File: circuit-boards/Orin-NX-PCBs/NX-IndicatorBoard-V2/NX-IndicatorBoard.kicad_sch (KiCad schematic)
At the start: 12 parts, among them J1 NX Expansion, J2 CAN1, J3 CAN1, J4 CAN2, J5 CAN2, J6 PC LED, P1 Samtec 40 pin Elevated Socket

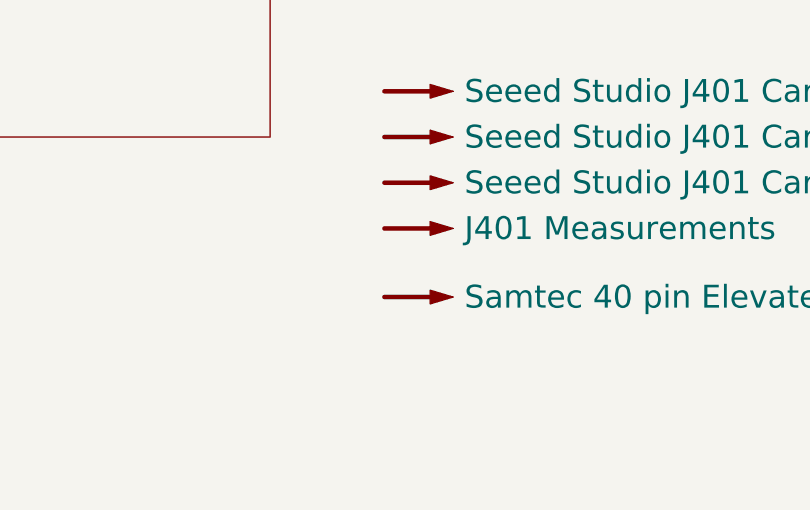
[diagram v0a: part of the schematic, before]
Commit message: Check in of NX Adapter and Indicator boards.  Complete pending review
Signed-off-by: Scott <sgberman1@gmail.com>
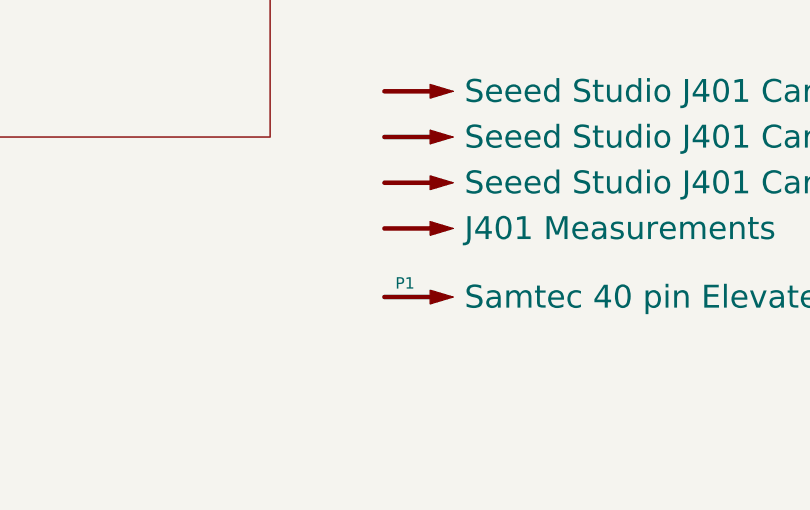
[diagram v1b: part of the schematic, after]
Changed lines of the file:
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@@
 	(title_block
 		(title "NX Indicator Board V2")
-		(date "2024-07-14")
+		(date "2024-07-21")
 		(rev "2")
 		(company "971 Spartan Robotics")
@@
 		(dnp no)
 		(property "Reference" "P1"
-			(at 237.49 199.644 0)
-			(effects
-				(font
-					(size 1.27 1.27)
-				)
-				(hide yes)
-			)
-		)
+			(at 235.966 200.406 0)
+			(effects
+				(font
+					(size 1.27 1.27)
+				)
+			)
+		)

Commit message: Intermediate checkin of NX-Indicator-board
Signed-off-by: Scott Berman <scott.berman@bluerivertech.com>
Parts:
- removed H1, H4: MountingHole, MountingHole:MountingHole_2.7mm_M2.5_Pad, symbol Mechanical:MountingHole
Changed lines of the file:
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@@
-	)
-	(symbol
-		(lib_id "Mechanical:MountingHole")
-		(at 148.59 200.66 0)
-		(unit 1)
-		(exclude_from_sim no)
-		(in_bom no)
-		(on_board yes)
-		(dnp no)
-		(fields_autoplaced yes)
-		(property "Reference" "H4"
-			(at 151.13 199.39 0)
-			(effects
-				(font
-					(size 1.27 1.27)
-				)
-				(justify left)
-			)
-		)
-		(property "Value" "MountingHole"
-			(at 151.13 201.93 0)
-			(effects
-				(font
-					(size 1.27 1.27)
-				)
-				(justify left)
-			)
-		)
-		(property "Footprint" "MountingHole:MountingHole_2.7mm_M2.5_Pad"
-			(at 148.59 200.66 0)
-			(effects
-				(font
-					(size 1.27 1.27)
-				)
-				(hide yes)
-			)
-		)
-		(property "Datasheet" "~"
-			(at 148.59 200.66 0)
-			(effects
-				(font
-					(size 1.27 1.27)
-				)
-				(hide yes)
-			)
-		)
-		(property "Description" ""
-			(at 148.59 200.66 0)
-			(effects
-				(font
-					(size 1.27 1.27)
-				)
-				(hide yes)
-			)
-		)
-		(instances
-			(project "NX-IndicatorBoard"
-				(path "/b2b9b2ba-ad3f-4e65-98f2-b291a62e1006"
-					(reference "H4")
-					(unit 1)
-				)
-			)
-		)
 	)
 	(symbol
@@
 					(unit 1)
 				)
-			)
-		)
-	)
-	(symbol
-		(lib_id "Mechanical:MountingHole")
-		(at 148.59 194.31 0)
-		(unit 1)
-		(exclude_from_sim no)
-		(in_bom no)
-		(on_board yes)
-		(dnp no)
-		(fields_autoplaced yes)
-		(property "Reference" "H1"
-			(at 151.13 193.04 0)
-			(effects
-				(font
-					(size 1.27 1.27)
-				)
-				(justify left)
-			)
-		)
-		(property "Value" "MountingHole"
-			(at 151.13 195.58 0)
-			(effects
-				(font
-					(size 1.27 1.27)
-				)
-				(justify left)
-			)
-		)
-		(property "Footprint" "MountingHole:MountingHole_2.7mm_M2.5_Pad"
-			(at 148.59 194.31 0)
-			(effects
-				(font
-					(size 1.27 1.27)
-				)
-				(hide yes)
-			)
-		)
-		(property "Datasheet" "~"
-			(at 148.59 194.31 0)
-			(effects
-				(font
-					(size 1.27 1.27)
-				)
-				(hide yes)
-			)
-		)
-		(property "Description" ""
-			(at 148.59 194.31 0)
-			(effects
-				(font
-					(size 1.27 1.27)
-				)
-				(hide yes)
-			)
-		)
-		(instances
-			(project "NX-IndicatorBoard"
-				(path "/b2b9b2ba-ad3f-4e65-98f2-b291a62e1006"
-					(reference "H1")
-					(unit 1)
-				)

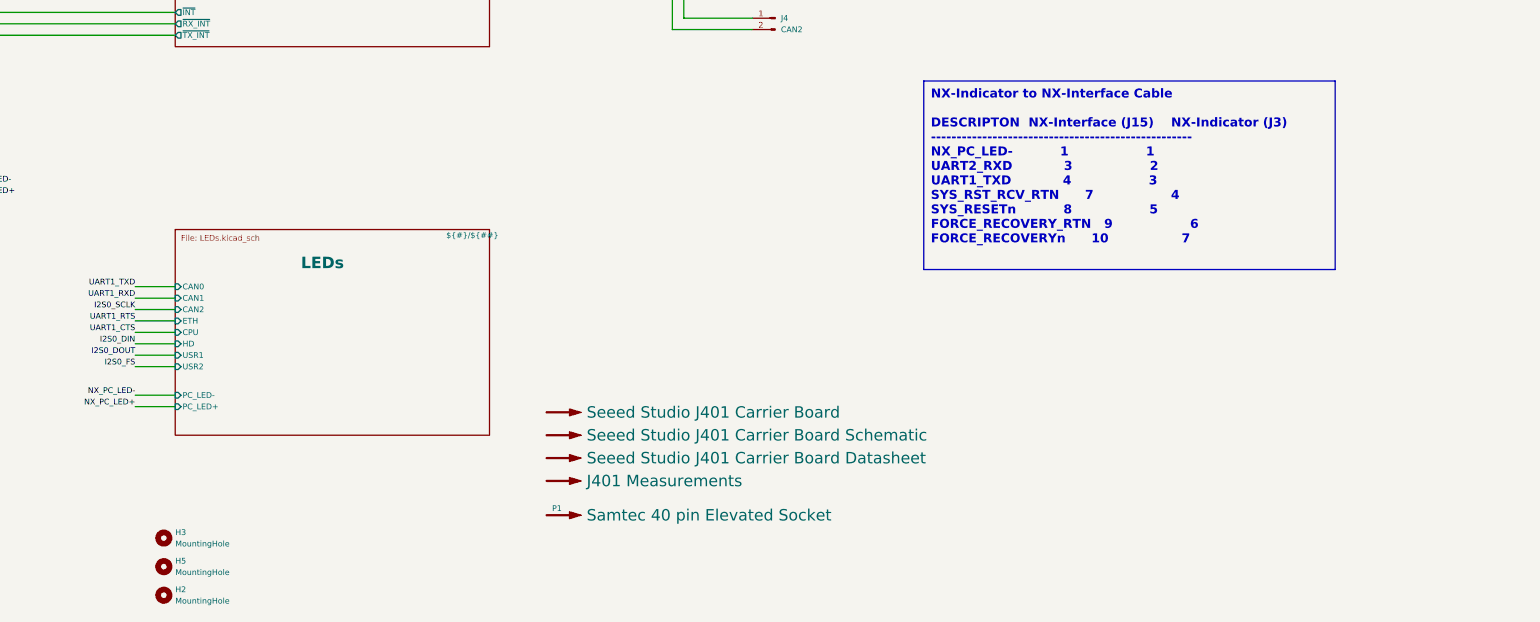
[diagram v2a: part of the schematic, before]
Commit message: Checkin of NX Indicator board 2x CAN FD + 6 LEDs
Signed-off-by: Scott <sgberman1@gmail.com>
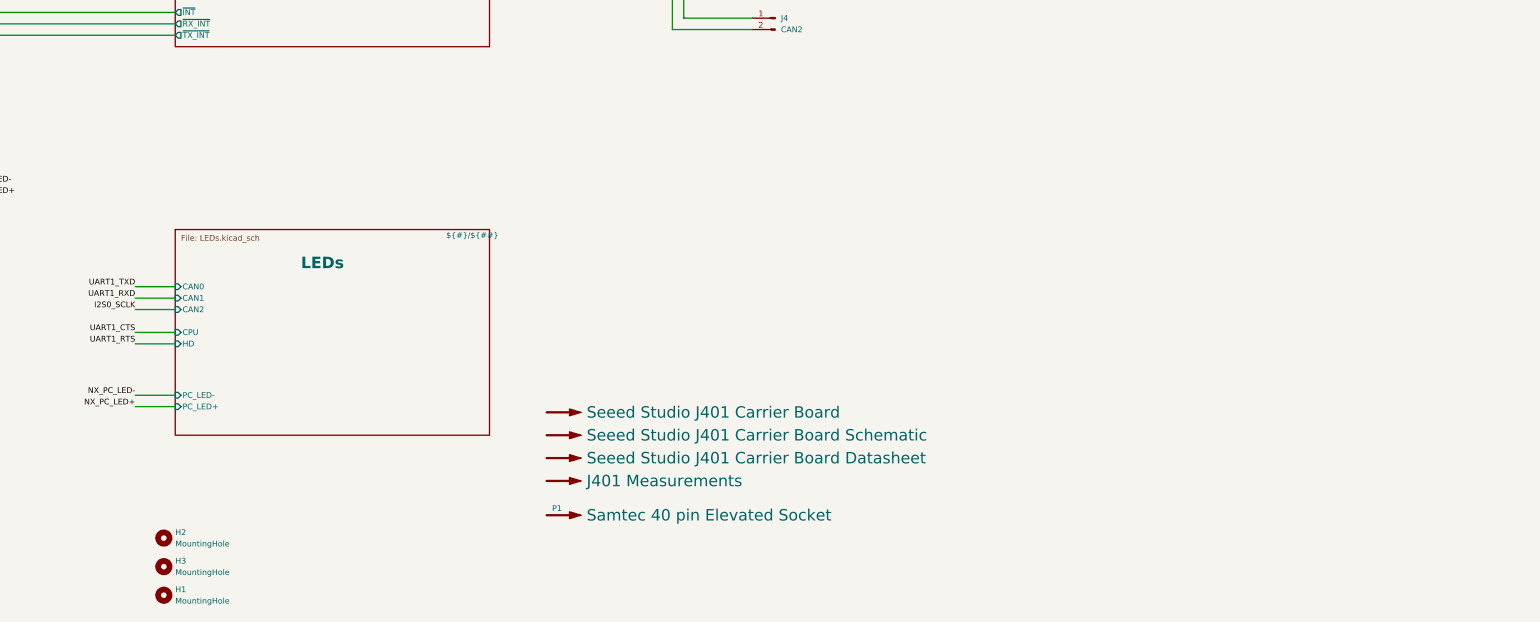
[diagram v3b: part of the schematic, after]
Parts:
- renumbered H2 to H1, H3 to H2, H5 to H3
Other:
- sheet LEDs ports: added none; removed ETH, USR1, USR2
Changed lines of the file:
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@@
 	(title_block
 		(title "NX Indicator Board V2")
-		(date "2024-07-21")
+		(date "2024-07-28")
 		(rev "2")
 		(company "971 Spartan Robotics")
@@
 	(wire
 		(pts
-			(xy 142.24 168.91) (xy 151.13 168.91)
-		)
-		(stroke
-			(width 0)
-			(type default)
-		)
-	)
-	(wire
-		(pts
 			(xy 261.62 86.36) (xy 279.4 86.36)
 		)
@@
 	(wire
 		(pts
-			(xy 142.24 158.75) (xy 151.13 158.75)
-		)
-		(stroke
-			(width 0)
-			(type default)
-		)
-	)
-	(wire
-		(pts
 			(xy 81.28 165.1) (xy 91.44 165.1)
 		)
@@
 	(wire
 		(pts
-			(xy 142.24 166.37) (xy 151.13 166.37)
-		)
-		(stroke
-			(width 0)
-			(type default)
-		)
-	)
-	(wire
-		(pts
 			(xy 104.14 40.64) (xy 151.13 40.64)
 		)
@@
 		)
 	)
-	(text_box "NX-Indicator to NX-Interface Cable\n\nDESCRIPTON  NX-Interface (J15)    NX-Indicator (J3)\n---------------------------------------------------\nNX_PC_LED-           1                  1\nUART2_RXD            3                  2\nUART1_TXD            4                  3\nSYS_RST_RCV_RTN      7                  4\nSYS_RESETn           8                  5\nFORCE_RECOVERY_RTN   9                  6\nFORCE_RECOVERYn      10                 7\n"
-		(exclude_from_sim no)
-		(at 317.5 105.41 0)
-		(size 91.44 41.91)
-		(stroke
-			(width 0)
-			(type default)
-		)
-		(fill
-			(type none)
-		)
-		(effects
-			(font
-				(face "FreeMono")
-				(size 2 2)
-				(bold yes)
-			)
-			(justify left top)
-		)
-	)
 	(label "I2C1_SCL"
 		(at 64.77 170.18 180)
@@
 		)
 	)
+	(label "UART1_RTS"
+		(at 142.24 163.83 180)
+		(fields_autoplaced yes)
+		(effects
+			(font
+				(size 1.27 1.27)
+			)
+			(justify right bottom)
+		)
+	)
 	(label "SPI1_CS0"
 		(at 104.14 86.36 180)
@@
 		)
 	)
-	(label "I2S0_FS"
-		(at 142.24 168.91 180)
-		(fields_autoplaced yes)
-		(effects
-			(font
-				(size 1.27 1.27)
-			)
-			(justify right bottom)
-		)
-	)
 	(label "SPI1_CS1"
 		(at 85.09 182.88 0)
@@
 		)
 	)
-	(label "I2S0_DIN"
-		(at 142.24 163.83 180)
-		(fields_autoplaced yes)
-		(effects
-			(font
-				(size 1.27 1.27)
-			)
-			(justify right bottom)
-		)
-	)
 	(label "CAN2_L"
 		(at 278.13 83.82 180)
@@
 		)
 	)
-	(label "I2S0_DOUT"
-		(at 142.24 166.37 180)
-		(fields_autoplaced yes)
-		(effects
-			(font
-				(size 1.27 1.27)
-			)
-			(justify right bottom)
-		)
-	)
 	(label "NX_PC_LED-"
 		(at 142.24 175.26 180)
@@
 		)
 	)
-	(label "UART1_RTS"
-		(at 142.24 158.75 180)
-		(fields_autoplaced yes)
-		(effects
-			(font
-				(size 1.27 1.27)
-			)
-			(justify right bottom)
-		)
-	)
 	(label "NX_PC_LED+"
 		(at 104.14 130.81 0)
@@
 		(dnp no)
 		(fields_autoplaced yes)
-		(property "Reference" "H5"
+		(property "Reference" "H3"
 			(at 151.13 212.09 0)
 			(effects
@@
 			(project "NX-IndicatorBoard"
 				(path "/b2b9b2ba-ad3f-4e65-98f2-b291a62e1006"
-					(reference "H5")
+					(reference "H3")
 					(unit 1)
 				)
@@
 		(dnp no)
 		(fields_autoplaced yes)
-		(property "Reference" "H2"
+		(property "Reference" "H1"
 			(at 151.13 218.44 0)
 			(effects
@@
 			(project "NX-IndicatorBoard"
 				(path "/b2b9b2ba-ad3f-4e65-98f2-b291a62e1006"
-					(reference "H2")
+					(reference "H1")
 					(unit 1)
 				)
@@
 		(dnp no)
 		(fields_autoplaced yes)
-		(property "Reference" "H3"
+		(property "Reference" "H2"
 			(at 151.13 205.74 0)
 			(effects
@@
 			(project "NX-IndicatorBoard"
 				(path "/b2b9b2ba-ad3f-4e65-98f2-b291a62e1006"
-					(reference "H3")
+					(reference "H2")
 					(unit 1)
 				)
@@
 			)
 		)
-		(pin "ETH" input
-			(at 151.13 158.75 180)
-			(effects
-				(font
-					(size 1.27 1.27)
-				)
-				(justify left)
-			)
-		)
 		(pin "CPU" input
 			(at 151.13 161.29 180)
@@
 			(effects
 				(font
-					(size 1.27 1.27)
-				)
-				(justify left)
-			)
-		)
-		(pin "USR1" input
-			(at 151.13 166.37 180)
-			(effects
-				(font
-					(size 1.27 1.27)
-				)
-				(justify left)
-			)
-		)
-		(pin "USR2" input
-			(at 151.13 168.91 180)
-			(effects
-				(font

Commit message: Minor BOM fix
Signed-off-by: Scott Berman <scott.berman@bluerivertech.com>
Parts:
- J2, J4: MFG P/N 70555-0036 -> 0705550036
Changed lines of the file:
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@@
 			)
 		)
-		(property "MFG P/N" "70555-0036"
+		(property "MFG P/N" "0705550036"
 			(at 284.48 91.44 0)
 			(effects
@@
 			)
 		)
-		(property "MFG P/N" "70555-0036"
-			(at 284.48 53.34 0)
-			(effects
+		(property "MFG P/N" "0705550036"
+			(at 284.48 53.34 0)
+			(effects
